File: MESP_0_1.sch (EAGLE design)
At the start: 5 parts, among them U1 LSM9DS1

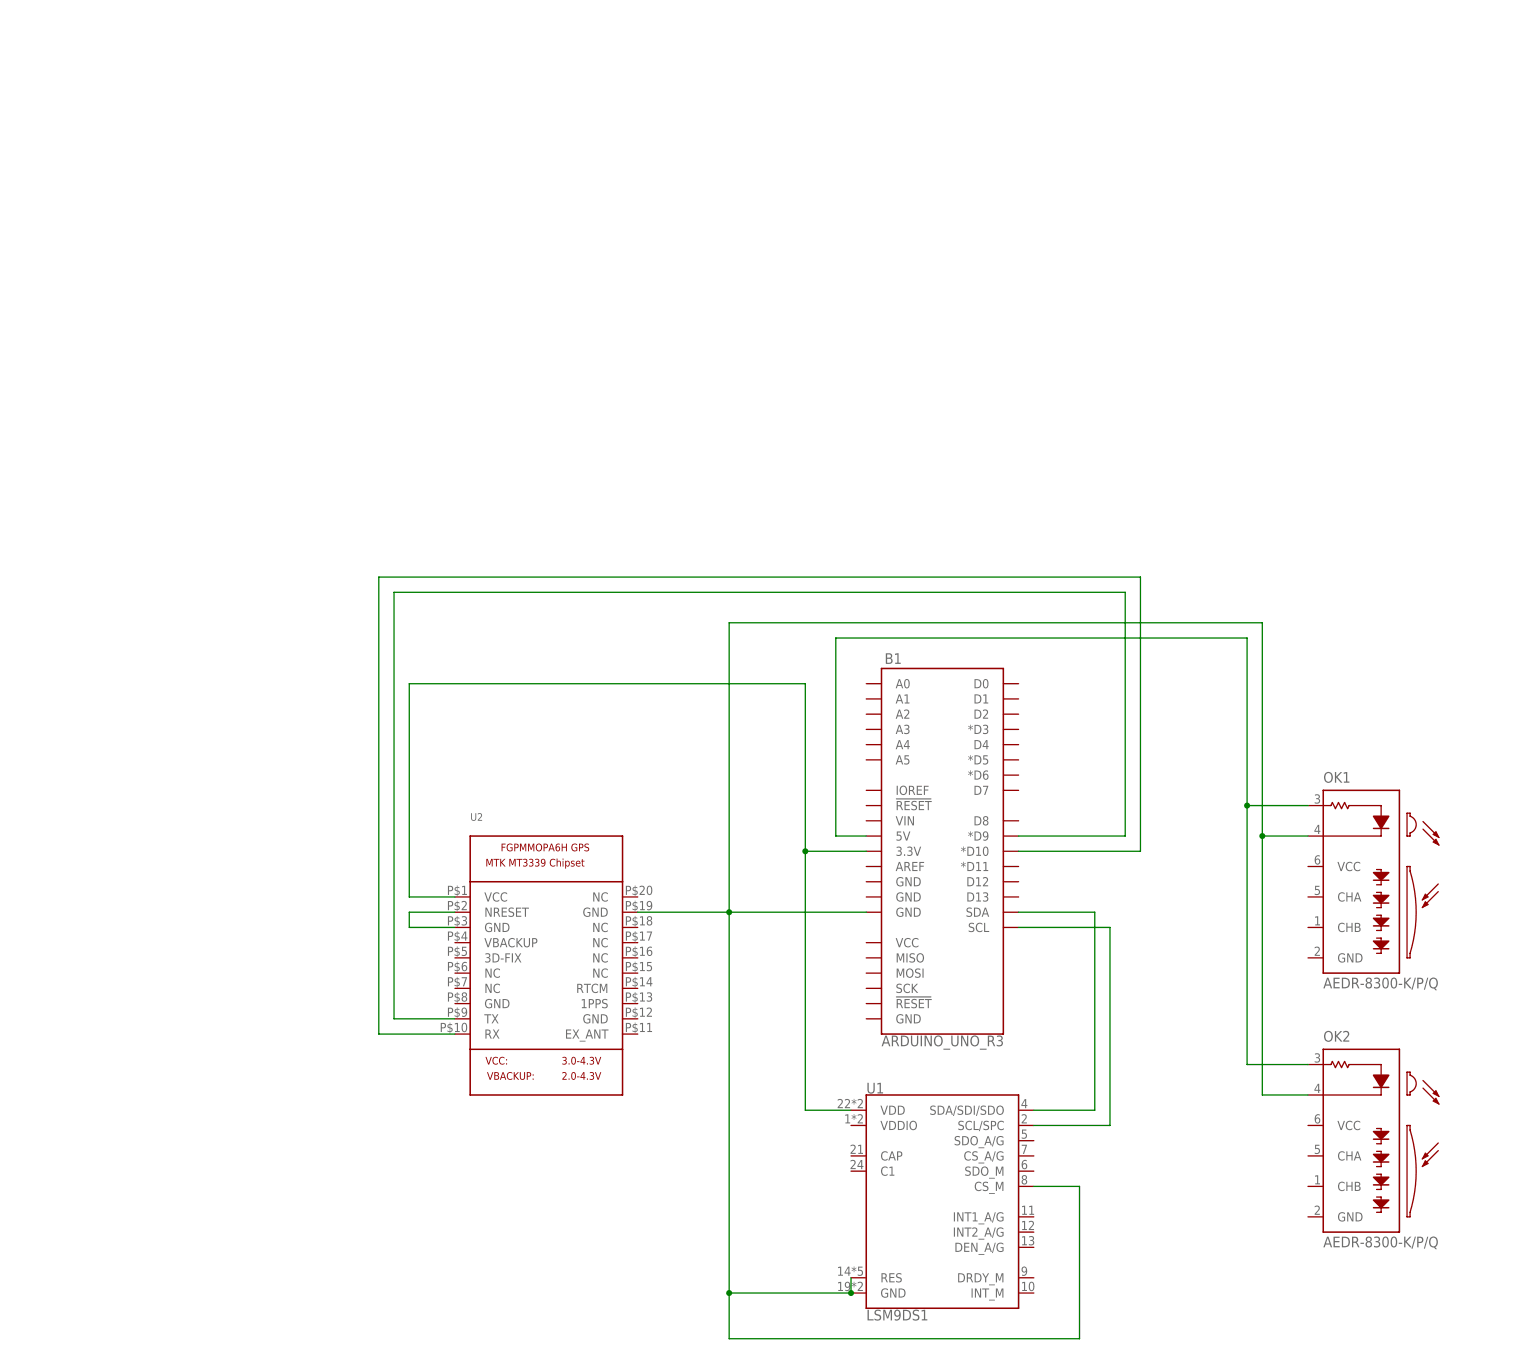
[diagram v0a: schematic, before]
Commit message: Finished Schematic Overview Drawing for CDR
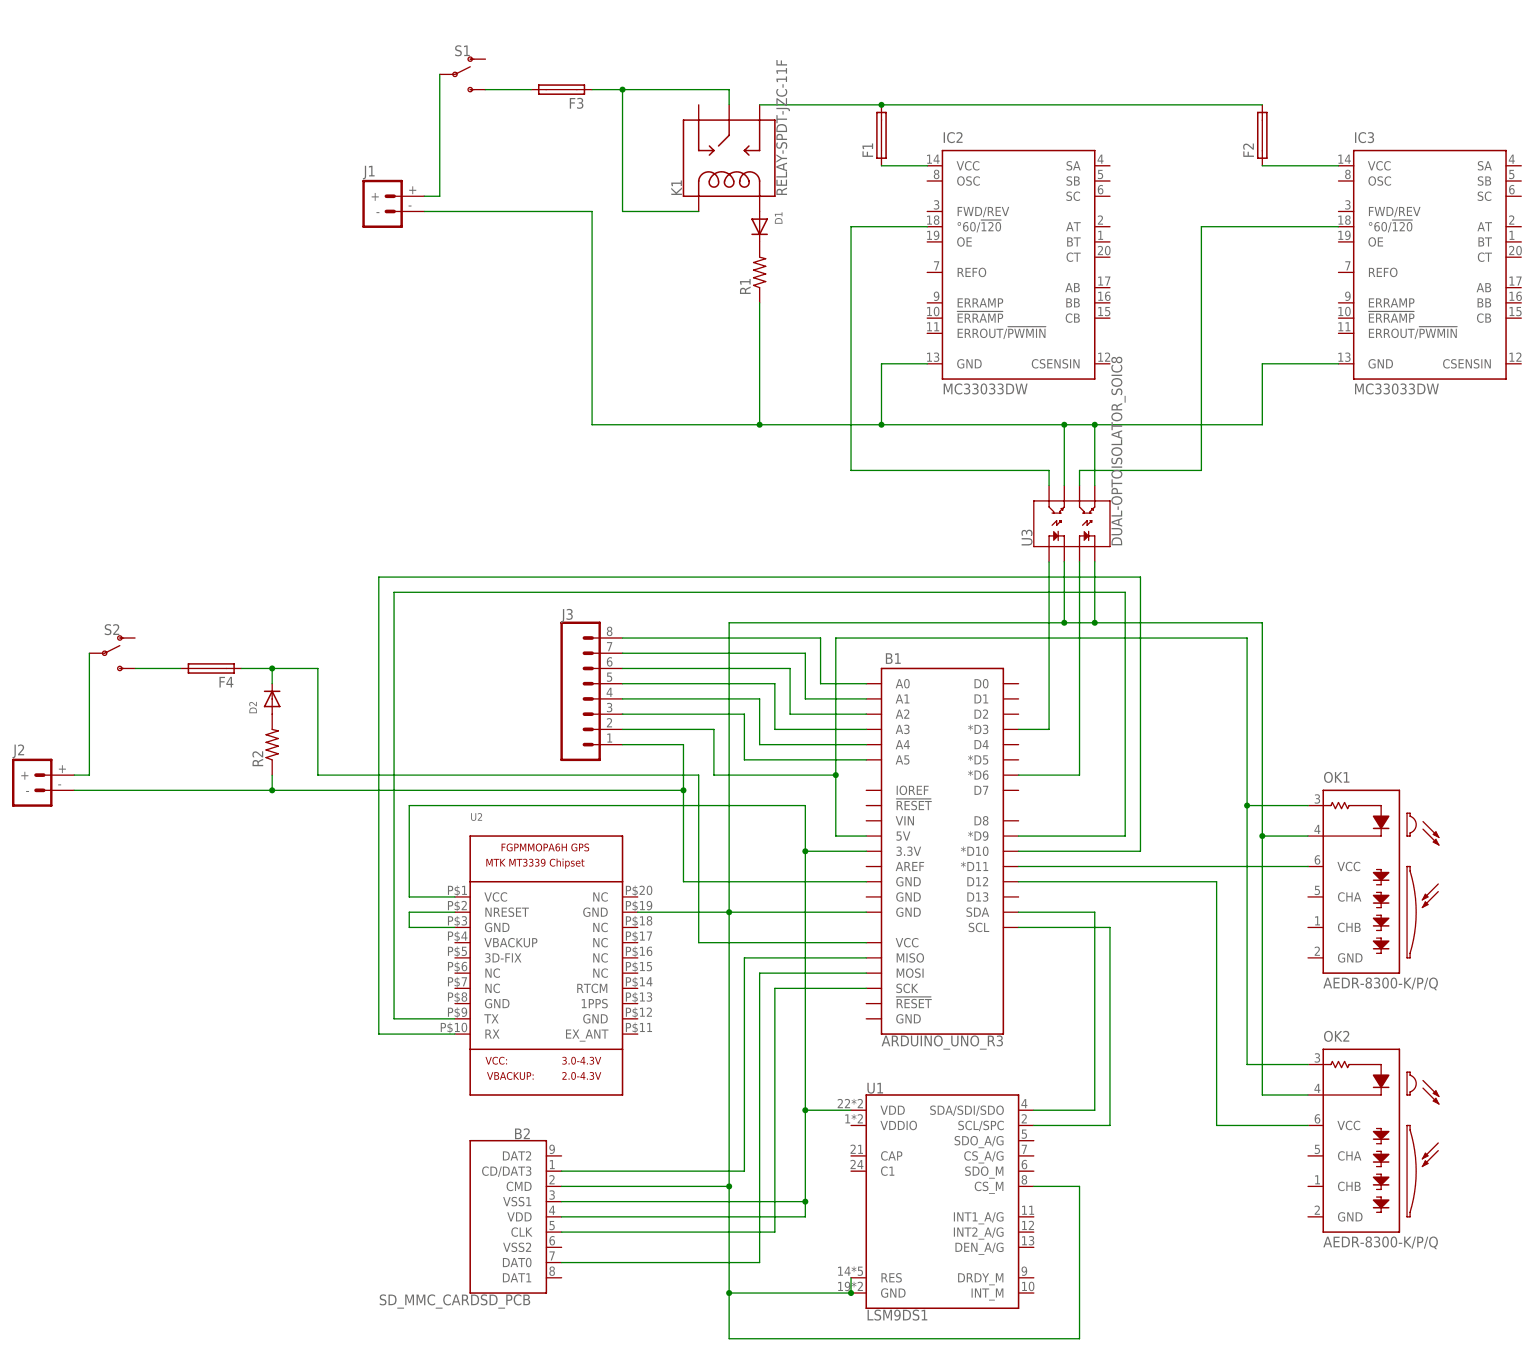
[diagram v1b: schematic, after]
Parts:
- added B2: SD_MMC_CARDSD_PCB, SparkFun-Boards:SD_MMC_CARDSD_PCB
- added D1, D2: (no value), Adafruit Ultimate GPS:ADAFRUIT_DIODEDO-1N4148
- added F1, F2: (no value), fuse:TE5
- added F3, F4: (no value), fuse:19559
- added IC2, IC3: MC33033DW, motorola-sensor-driver:MC33033DW
- added J1, J2: (no value), SparkFun-Connectors:BATTERY_CONN_DEANS
- added J3: (no value), SparkFun-Connectors:CONN_08LONGPADS
- added K1: RELAY-SPDT-JZC-11F, SparkFun-Electromechanical:RELAY-SPDT-JZC-11F
- added R1, R2: (no value), MESP_0_1:R-US_0204/2V
- added S1, S2: (no value), SparkFun-Switches:SWITCH-SPDT-PTH-11.6X4.0MM
- added U3: DUAL-OPTOISOLATOR_SOIC8, SparkFun-DiscreteSemi:DUAL-OPTOISOLATOR_SOIC8
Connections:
- removed net N$9: B1.5V, OK1G$1.A, OK2G$1.A
- new net N$1: B1.*D11, OK1G$1.VCC
- new net N$10: B1.D12, OK2G$1.VCC
- new net N$11: F1.1, IC2.VCC
- new net N$12: IC2.GND, IC3.GND, J1.-, R1.1, U3.EM1, U3.EM2
- new net N$13: F2.1, IC3.VCC
- new net N$14: F1.2, F2.2, K1.NO
- new net N$15: F3.1, K1.COIL1, K1.MAIN
- new net N$16: D1.A, K1.COIL2
- new net N$17: D1.C, R1.2
- new net N$18: F3.2, S1.S
- new net N$19: J1.+, S1.P
- new net N$20: IC2.°60/!120, U3.CL1
- new net N$21: IC3.°60/!120, U3.CL2
- new net N$22: B1.*D6, U3.A2
- new net N$23: B1.*D3, U3.A1
- new net N$24: B1.MOSI, B2.DAT0
- new net N$25: B1.SCK, B2.CLK
- new net N$26: B1.MISO, B2.CD/DAT3
- new net N$27: B1.A0, J3.8
- new net N$28: D2.A, R2.2
- new net N$29: B1.GND@2, J2.-, J3.1, R2.1
- new net N$30: B1.VCC, D2.C, F4.1
- new net N$31: B1.A1, J3.7
- new net N$32: F4.2, S2.S
- new net N$33: J2.+, S2.P
- new net N$34: B1.A2, J3.6
- new net N$35: B1.A3, J3.5
- new net N$36: B1.A4, J3.4
- new net N$37: B1.A5, J3.3
- new net N$38: B1.5V, J3.2, OK1G$1.A, OK2G$1.A
- net N$2: now also B2.VDD, B2.VSS1
- net N$8: now also B2.CMD, U3.C1, U3.C2
